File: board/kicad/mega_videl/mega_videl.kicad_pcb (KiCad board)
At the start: 10 copper layers, 67.6 x 89 mm, 248 parts, among them J1 Conn_02x07_Odd_Even, J2 Conn_01x04, J3 FPGA JTAG, J4 Conn_01x04, J5 Conn_02x25_Odd_Even, J6 Conn_02x25_Odd_Even, U1 TPS51200DRCR, U10 5CGXFC5C6F23I7N, U11 TXV0108RGYR, U12 USB3300-EZK, U13 AP2553AW6-7, U14 PI6CG33201CZDIEX, U15 LAN9220-ABZJ, U16 PCA9546APWR, U17 HC-USB3.0-L168-WP, U18 CDCBT1001DPWR, U19 N25Q/MT25Q, U2 MT41K256M16LY, U20 TMDS1204IRNQR, U21 TPD4E02B04DQA, U22 TPD4E02B04DQA, U3 MT41K256M16LY, U4 TPS62903RPJR, U5 SN74LVC3G34DCUR, U6 TPS7A2025PDBVR, U7 TXB0104RGYR, U8 TPS62903RPJR, U9 74.25MHz, Y1 24MHz, Y2 25MHz, Y3 25MHz, Y4 ASE-50MHz

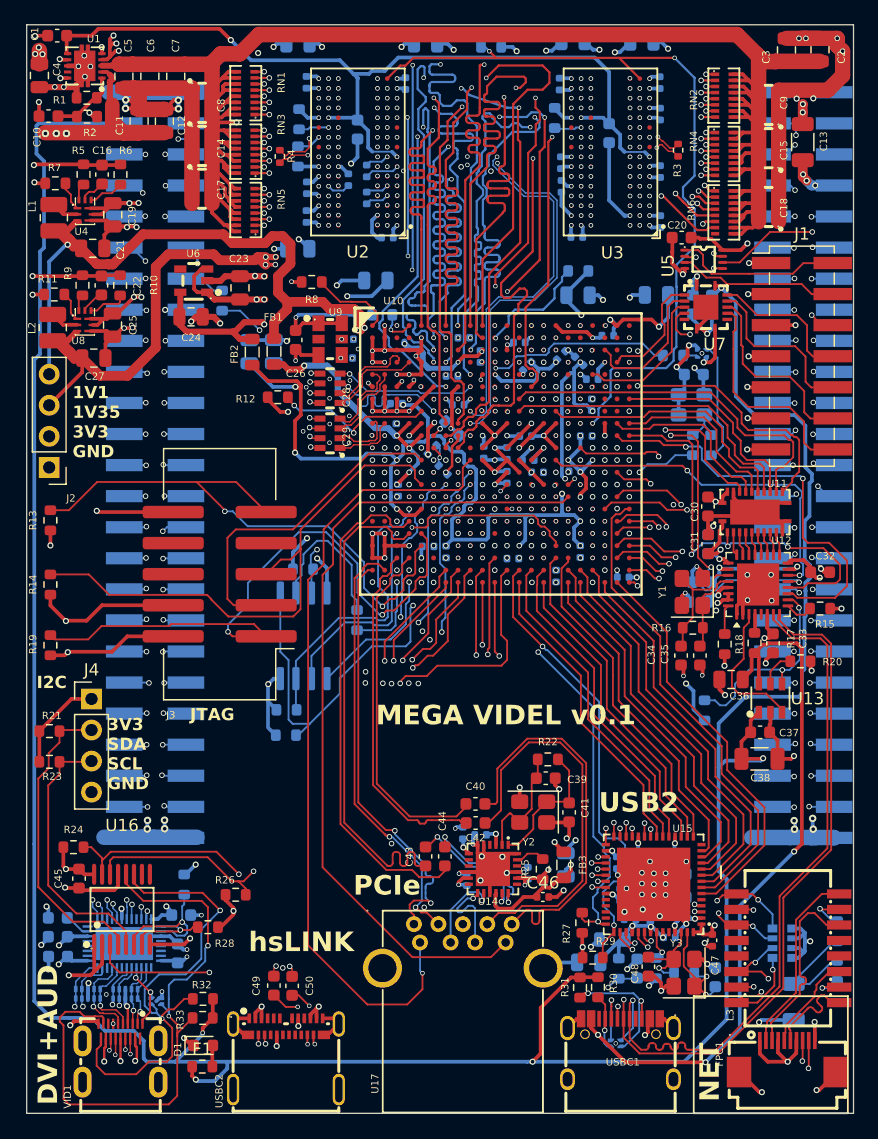
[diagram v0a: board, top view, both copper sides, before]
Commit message: Assigned all parts with JLCPCB plugin
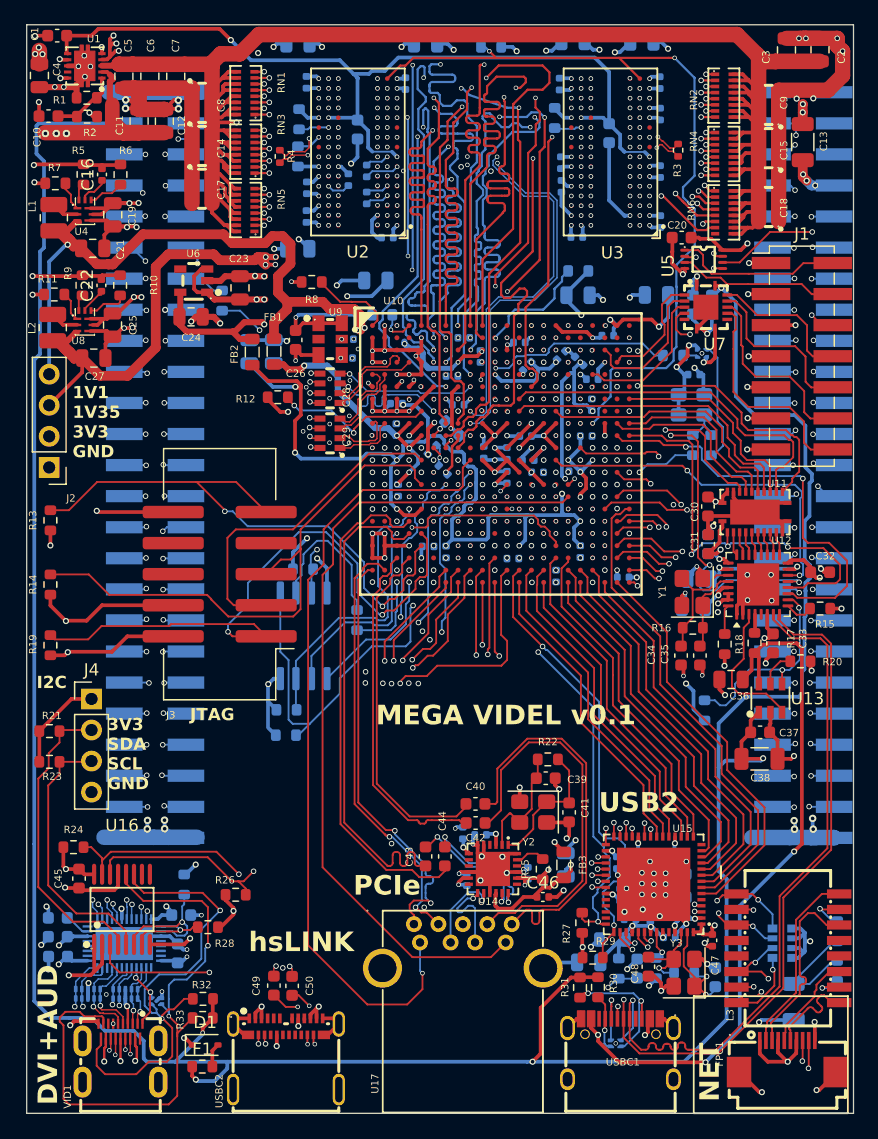
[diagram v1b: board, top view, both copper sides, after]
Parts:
- C113, C114: footprint Capacitor_SMD:C_0603_1608Metric -> Capacitor_SMD:C_0805_2012Metric
- C124, C127: value 0.01uF -> 10nF
- C16, C22, C90: footprint Capacitor_SMD:C_0603_1608Metric -> Capacitor_SMD:C_0402_1005Metric
- C34, C35: value 22pF -> 30pF
- C38: value 120uF -> 100uF
- D1: footprint Diode_SMD:D_0603_1608Metric -> Diode_SMD:D_SOD-323
- R11, R7: value 47k -> 10k
- moved C114 0.56 mm to (84.0, 71.6)
- moved C113 0.35 mm to (84.5, 69.3)
- moved D1 0.16 mm to (44.1, 107.4)
